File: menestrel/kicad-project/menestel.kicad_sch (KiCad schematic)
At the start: 31 parts, among them J1 Conn_01x01, J2 Conn_01x01, SW1 ПД11-5, U13 К155ЛА3, X1 СНП58-64, X2 СГ-3

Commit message: Правка мелких косяков Менестреля rev1
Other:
- note added: "СГ-5, пин 3"
- note added: "СГ-5, пин 5"
- note removed: "СГ-3, пин 3"
- note removed: "СГ-3, пин 5"
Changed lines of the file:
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@@
   (title_block
     (title "Реплика \"Менестреля\" ::: https://eax.me/menestrel/")
-    (date "2023-06-18")
-    (rev "1")
+    (date "2023-06-23")
+    (rev "2")
   )
   (junction (at 208.28 64.135) (diameter 0) (color 0 0 0 0)
@@
     (stroke (width 0) (type default))
   )
-  (text "СГ-3, пин 3" (at 257.81 73.025 0)
+  (text "СГ-5, пин 3" (at 257.81 73.025 0)
     (effects (font (size 1.27 1.27)) (justify left bottom))
   )
-  (text "СГ-3, пин 5" (at 258.445 96.52 0)
+  (text "СГ-5, пин 5" (at 258.445 96.52 0)
     (effects (font (size 1.27 1.27)) (justify left bottom))
   )

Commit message: Схема и gerber-файлы Менестреля rev2
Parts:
- X2: value СГ-3 -> СГ-5
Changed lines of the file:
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@@
       (effects (font (size 1.27 1.27)) (justify right))
     )
-    (property "Value" "СГ-3" (at 262.89 86.3599 90)
-      (effects (font (size 1.27 1.27)) (justify right))
+    (property "Value" "СГ-5" (at 262.89 86.3599 90)
+      (effects (font (size 1.27 1.27)) (justify right) hide)
     )
     (property "Footprint" "Connector_PinHeader_2.54mm:PinHeader_1x03_P2.54mm_Vertical" (at 256.54 85.09 0)

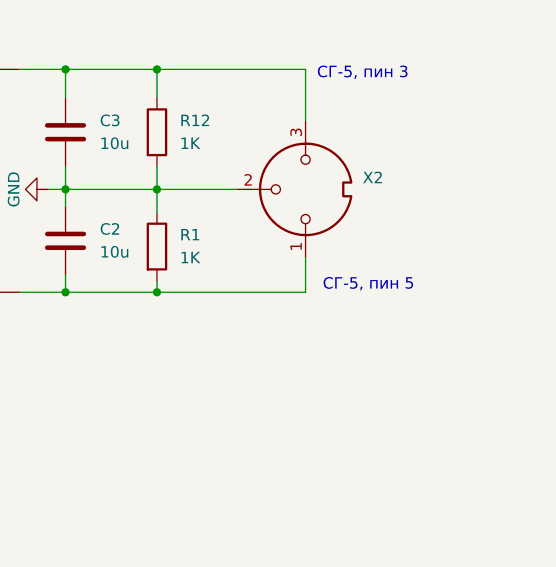
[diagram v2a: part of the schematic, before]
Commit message: Поправлен мелкий косяк в схеме "Менестреля"
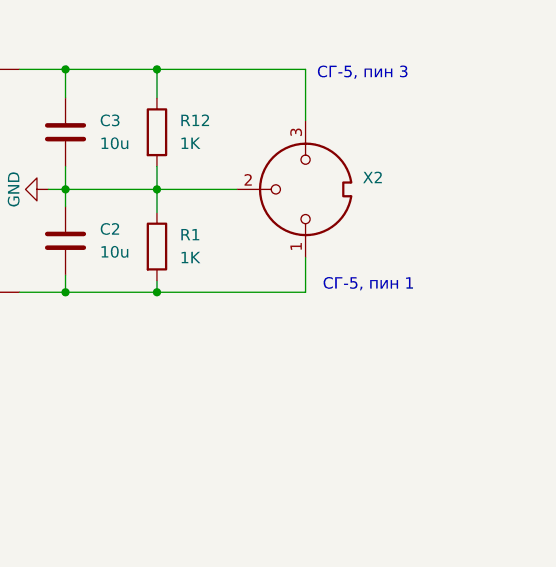
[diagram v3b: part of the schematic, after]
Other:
- note added: "СГ-5, пин 1"
- note removed: "СГ-5, пин 5"
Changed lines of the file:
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@@
     (effects (font (size 1.27 1.27)) (justify left bottom))
   )
-  (text "СГ-5, пин 5" (at 258.445 96.52 0)
+  (text "СГ-5, пин 1" (at 258.445 96.52 0)
     (effects (font (size 1.27 1.27)) (justify left bottom))
   )

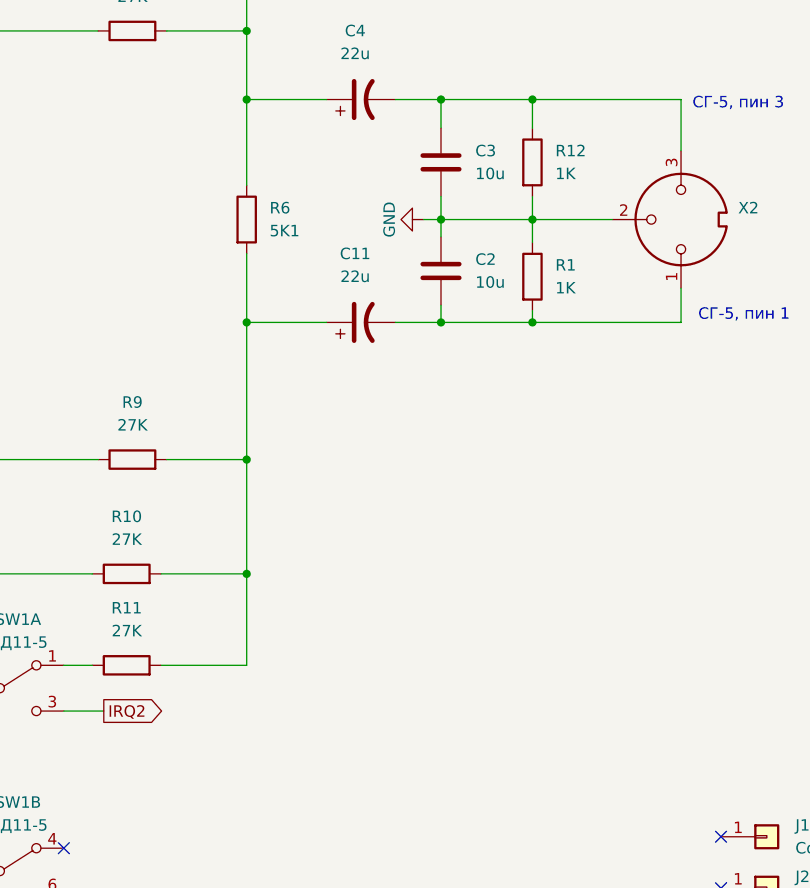
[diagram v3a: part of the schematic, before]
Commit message: Менестрель: исправлены номиналы C2 и C3 (u10 = 0.1 мкФ, не 10 мкФ)
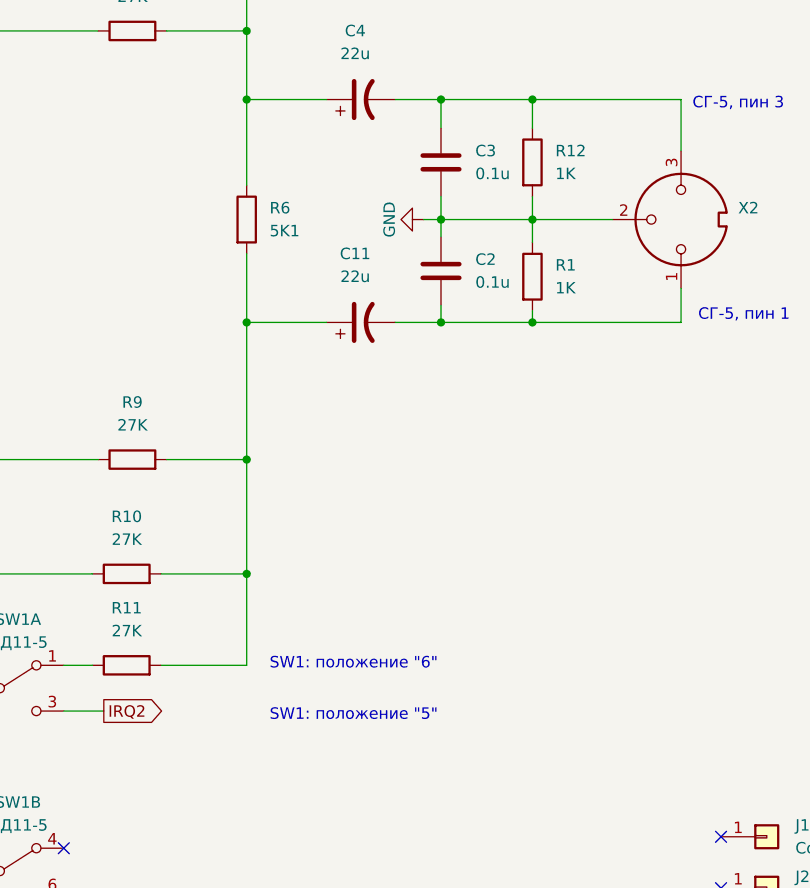
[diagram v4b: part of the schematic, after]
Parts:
- C2, C3: value 10u -> 0.1u
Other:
- note added: "SW1: положение "5""
- note added: "SW1: положение "6""
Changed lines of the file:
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@@
+    (effects (font (size 1.27 1.27)) (justify left bottom))
+  )
+  (text "SW1: положение \"6\"" (at 210.82 135.255 0)
+    (effects (font (size 1.27 1.27)) (justify left bottom))
+  )
+  (text "SW1: положение \"5\"" (at 210.82 140.97 0)
     (effects (font (size 1.27 1.27)) (justify left bottom))
   )
@@
       (effects (font (size 1.27 1.27)) (justify left))
     )
-    (property "Value" "10u" (at 233.68 92.075 0)
+    (property "Value" "0.1u" (at 233.68 92.075 0)
       (effects (font (size 1.27 1.27)) (justify left))
     )
@@
       (effects (font (size 1.27 1.27)) (justify left))
     )
-    (property "Value" "10u" (at 233.68 80.01 0)
-      (effects (font (size 1.27 1.27)) (justify left))
-    )
+    (property "Value" "0.1u" (at 233.68 80.01 0)
+      (effects (font (size 1.27 1.27)) (justify left))
+    )
